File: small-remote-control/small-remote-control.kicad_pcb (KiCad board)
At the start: 2 copper layers, 75 x 10 mm, 10 parts, among them J1 AudioJack4, J2 AudioJack4, SW1 A, SW2 B, SW3 C, SW4 D

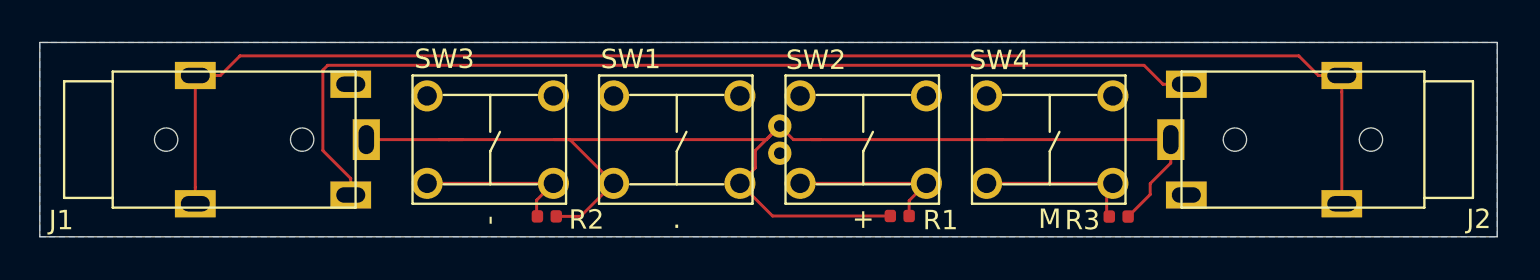
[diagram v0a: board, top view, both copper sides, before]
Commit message: removed feedthrough jack and moved switches closer
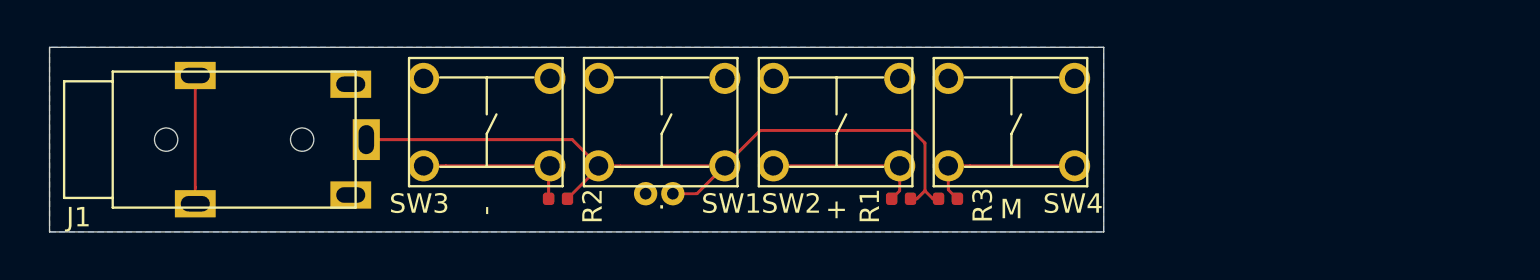
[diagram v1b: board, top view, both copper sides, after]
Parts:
- removed J2: AudioJack4, SW-Tensility:54-00174
- moved R3 8.83 mm to (157.7, 106.0), turned to 180 degrees
- moved MK1 6.14 mm to (142.9, 105.3), turned to 270 degrees
- moved SW4 2.17 mm to (161.0, 102.1)
- moved SW2 1.64 mm to (152.0, 102.1)
- moved SW1 1.19 mm to (143.0, 102.1)
- moved R2 1.07 mm to (137.7, 106.0)
- moved SW3 0.92 mm to (134.0, 102.1)
- moved R1 0.89 mm to (155.3, 106.0), turned to 0 degrees
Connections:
- J1 pad R1: /RIGHT -> (no net)
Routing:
- net /LEFT: track 73.0 -> 6.60 mm
- net /RIGHT: track 52.0 -> 0.00 mm
- net /MIC: track 69.2 -> 40.2 mm
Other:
- board size 75 x 10 mm -> 54.2 x 9.5 mm

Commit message: removed mic and switch D, added 2.2kΩ resistor
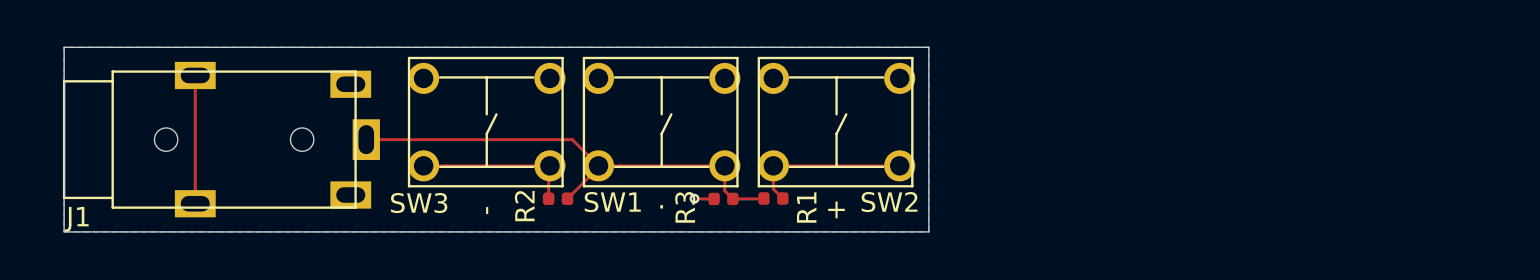
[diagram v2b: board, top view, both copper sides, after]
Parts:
- removed MK1: Microphone, SW-CUI-INC:CMC-4015-40P
- removed SW4: D, SW-Omron:B3W-6x6mm-NG
- R3: value 143Ω ±0.1% -> 2k21Ω ±0.1%
- moved R3 11.6 mm to (146.2, 106.0), turned to 0 degrees
- moved R1 6.57 mm to (148.8, 106.0), turned to 180 degrees
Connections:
- R3 pad 1: Net-(R3-Pad1) -> /GND
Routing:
- net /MIC: track 40.2 -> 24.8 mm
- net Net-(R3-Pad1): track 8.39 -> 0.00 mm
- net /GND: track 0.00 -> 1.01 mm, vias 0 -> 1
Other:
- board size 54.2 x 9.5 mm -> 44.5 x 9.5 mm
- board text removed: "M"

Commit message: switched to 0603 resistors
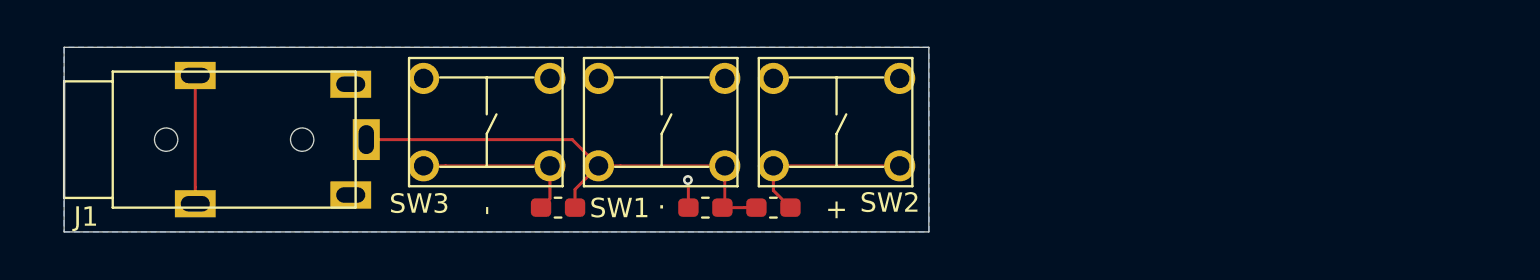
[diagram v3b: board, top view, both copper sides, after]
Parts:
- R1: value 267Ω ±0.1% -> 267Ω ±0.5%; footprint Resistor_SMD:R_0402_1005Metric -> Resistor_SMD:R_0603_1608Metric_Pad1.05x0.95mm_HandSolder
- R2: value 604Ω ±0.1% -> 604Ω ±0.5%; footprint Resistor_SMD:R_0402_1005Metric -> Resistor_SMD:R_0603_1608Metric_Pad1.05x0.95mm_HandSolder
- R3: value 2k21Ω ±0.1% -> 2k2Ω ±0.5%; footprint Resistor_SMD:R_0402_1005Metric -> Resistor_SMD:R_0603_1608Metric_Pad1.05x0.95mm_HandSolder
- moved R3 1.03 mm to (145.2, 106.5)
- moved R1 0.47 mm to (148.8, 106.5)
- moved R2 0.45 mm to (137.7, 106.5)
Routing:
- net /MIC: track 24.8 -> 25.6 mm
- net Net-(R1-Pad1): track 8.38 -> 9.01 mm
- net Net-(R2-Pad1): track 8.22 -> 8.84 mm
